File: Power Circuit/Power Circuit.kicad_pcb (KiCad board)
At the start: 2 copper layers, 24.4 x 21 mm, 32 parts, among them U1 TPS61087DRCT

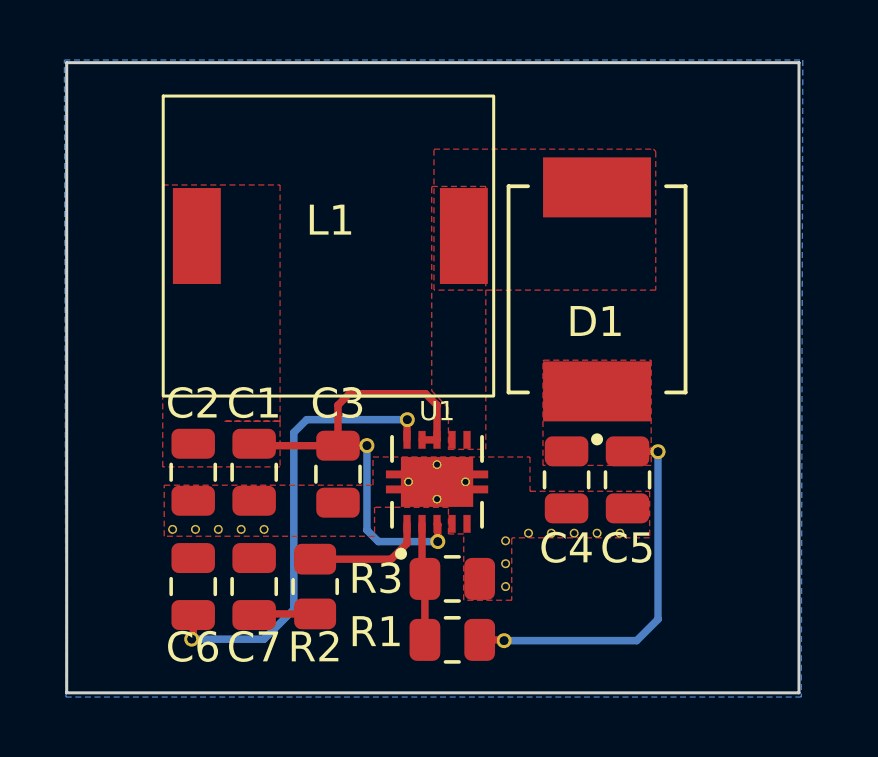
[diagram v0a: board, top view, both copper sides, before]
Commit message: added boost converter
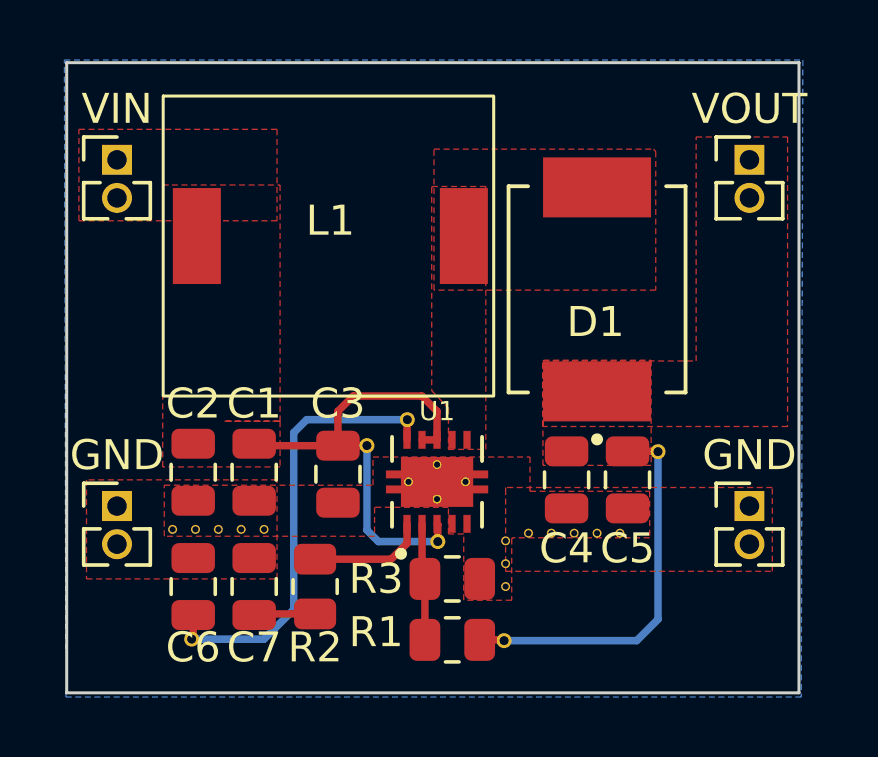
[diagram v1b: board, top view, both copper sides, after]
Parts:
- added GND: PinHeader_1x02_P1.27mm_Vertical, Connector_PinHeader_1.27mm:PinHeader_1x02_P1.27mm_Vertical, F.Cu at (67.3, 46.1)
- added GND: PinHeader_1x02_P1.27mm_Vertical, Connector_PinHeader_1.27mm:PinHeader_1x02_P1.27mm_Vertical, F.Cu at (88.4, 46.1)
- added VIN: PinHeader_1x02_P1.27mm_Vertical, Connector_PinHeader_1.27mm:PinHeader_1x02_P1.27mm_Vertical, F.Cu at (67.3, 34.5)
- added VOUT: PinHeader_1x02_P1.27mm_Vertical, Connector_PinHeader_1.27mm:PinHeader_1x02_P1.27mm_Vertical, F.Cu at (88.4, 34.5)
- C4, C5: value 47uf -> 10uf
